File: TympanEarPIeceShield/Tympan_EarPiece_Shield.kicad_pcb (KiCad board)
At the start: 4 copper layers, 38 x 40 mm, 49 parts, among them J1 Tympan_SJ-3523-SMT-TR, J2 Tympan_SJ-3524-SMT-TR-PI, J3 USB_B_Mini, J4 USB_B_Mini, J5 Conn_01x01, J6 Conn_01x01, P1 CONN_01X06, P2 CONN_01X06, P3 CONN_01X06, P4 CONN_01X06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

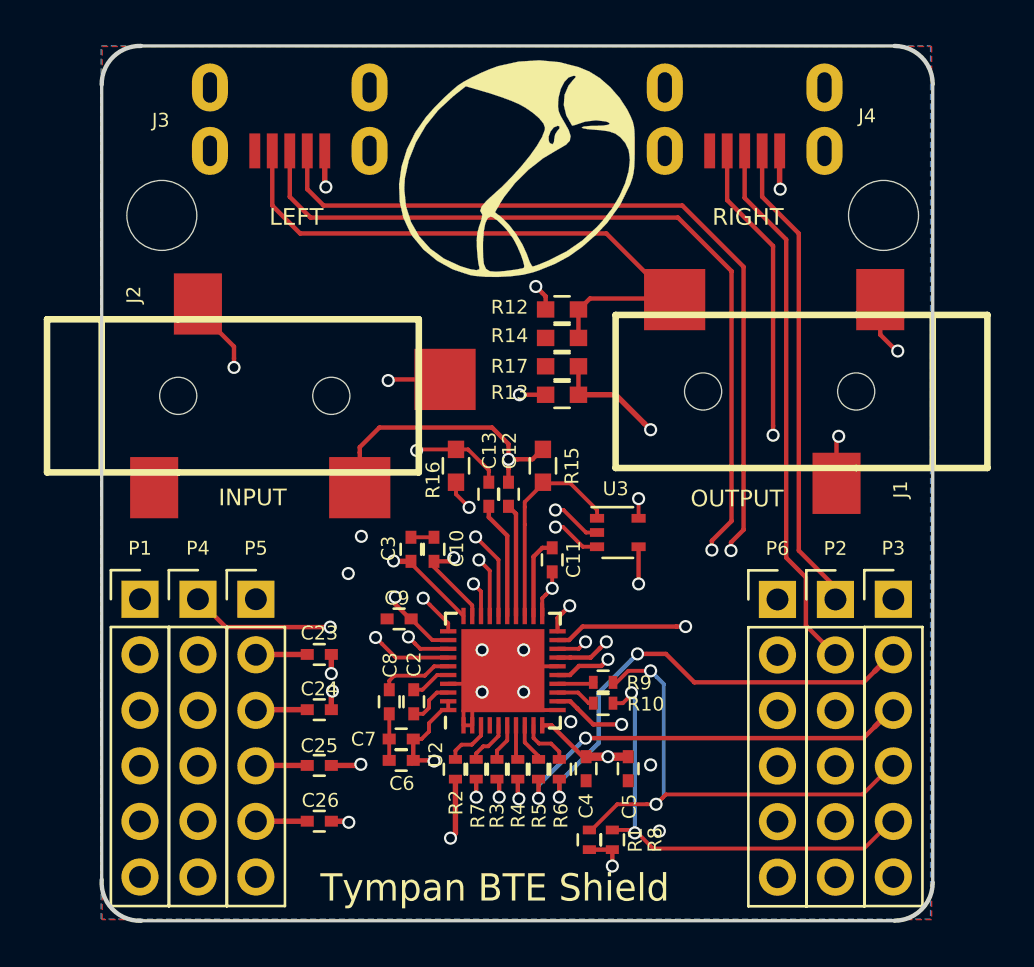
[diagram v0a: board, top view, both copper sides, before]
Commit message: Silk and audio jack positioning
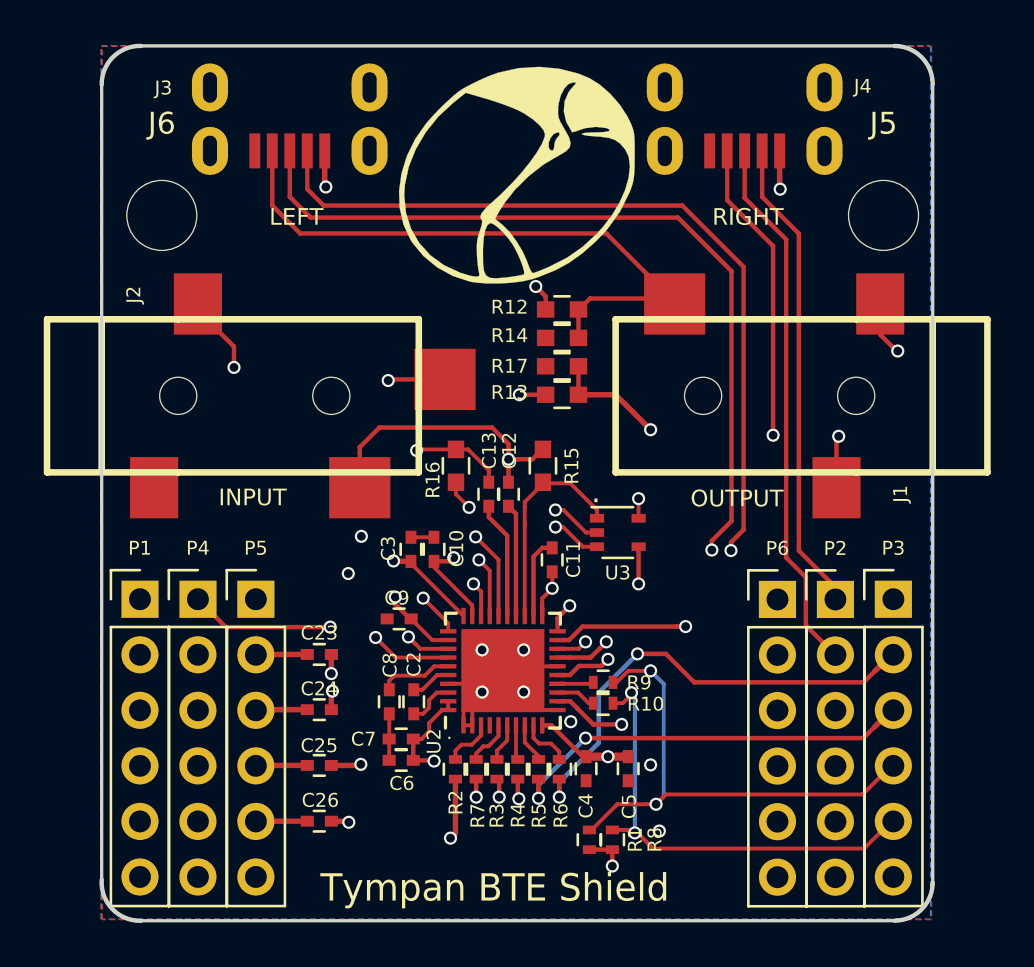
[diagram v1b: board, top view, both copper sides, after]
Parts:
- moved G*** 0.30 mm to (133.8, 52.4)
- moved J1 0.20 mm to (149.3, 62.5)
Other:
- board text added: "."
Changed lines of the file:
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@@
   (general
     (thickness 1.6)
-    (drawings 20)
+    (drawings 22)
     (tracks 496)
     (zones 0)
@@
   (layers
     (0 F.Cu signal)
-    (1 In1.Cu power)
-    (2 In2.Cu mixed)
-    (31 B.Cu signal)
+    (1 In1.Cu power hide)
+    (2 In2.Cu mixed hide)
+    (31 B.Cu signal hide)
     (32 B.Adhes user hide)
     (33 F.Adhes user hide)
     (34 B.Paste user)
     (35 F.Paste user)
-    (36 B.SilkS user)
+    (36 B.SilkS user hide)
     (37 F.SilkS user)
     (38 B.Mask user)
@@
   (module Tympan:USB_MINI_MOLEX_51387-0578 (layer F.Cu)
     (at 123.45 51.28)
-    (fp_text reference J3 (at -5.9 -1.4) (layer F.SilkS)
+    (fp_text reference J3 (at -5.775 -2.875) (layer F.SilkS)
       (effects (font (size 0.635 0.635) (thickness 0.127)))
     )
@@
   (module Tympan:USB_MINI_MOLEX_51387-0578 (layer F.Cu)
     (at 144.25 51.28)
-    (fp_text reference J4 (at 5.6 -1.6) (layer F.SilkS)
+    (fp_text reference J4 (at 5.4 -2.95) (layer F.SilkS)
       (effects (font (size 0.635 0.635) (thickness 0.127)))
     )
@@
   )
   (module Tympan:SJ-3523-SMT-TR (layer F.Cu)
-    (at 149.35 62.28 180)
+    (at 149.35 62.48 180)
     (attr smd)
     (fp_text reference J1 (at -2.032 -4.4831 90) (layer F.SilkS)
@@
   )
   (module Graphics:Tympan_LOGO (layer F.Cu)
-    (at 133.85 52.08)
+    (at 133.85 52.38)
     (attr smd)
     (fp_text reference G*** (at 0 0) (layer F.SilkS) hide
@@
     (tags "QFN 0.4")
     (attr smd)
-    (fp_text reference U2 (at -3.833 -3.0696 90) (layer F.SilkS)
+    (fp_text reference U2 (at -3.233 -3.1446 90) (layer F.SilkS)
       (effects (font (size 0.635 0.635) (thickness 0.127)))
     )
@@
     (tags "SOT-353 SC-70-5")
     (attr smd)
-    (fp_text reference U3 (at -0.1 -2) (layer F.SilkS)
+    (fp_text reference U3 (at 0 1.85) (layer F.SilkS)
       (effects (font (size 0.635 0.635) (thickness 0.127)))
     )
@@
     (tags "mounting hole 3.2mm no annular m3")
     (attr virtual)
-    (fp_text reference J5 (at 0.95 -2.85) (layer F.Fab)
+    (fp_text reference J5 (at 0 -4.2) (layer F.SilkS)
       (effects (font (size 1 1) (thickness 0.15)))
     )
@@
     (tags "mounting hole 3.2mm no annular m3")
     (attr virtual)
-    (fp_text reference J6 (at -1.65 -2.25) (layer F.Fab)
+    (fp_text reference J6 (at 0 -4.2) (layer F.SilkS)
       (effects (font (size 1 1) (thickness 0.15)))
     )
@@
     (pad 1 np_thru_hole circle (at 0 0) (size 3.2 3.2) (drill 3.2) (layers *.Cu *.Mask)
       (net 60 "Net-(J6-Pad1)"))
+  )
+  (gr_text . (at 130.75 77.88) (layer F.SilkS)
+    (effects (font (size 0.635 0.635) (thickness 0.127)))
+  )
+  (gr_text . (at 137.45 66.88) (layer F.SilkS)
+    (effects (font (size 1 1) (thickness 0.127)))
   )
   (gr_text LEFT (at 123.65 48.63) (layer B.SilkS)
@@
   (gr_line (start 151.1 46.48) (end 116.650536 46.479993) (angle 90) (layer Edge.Cuts) (width 0.15))
   (gr_line (start 152.85 84.73) (end 152.85 48.23) (angle 90) (layer Edge.Cuts) (width 0.15))
-  (gr_text "TYMPAN EARPIECE SHIELD" (at 133.85 69.28) (layer B.SilkS)
+  (gr_text "TYMPAN EARPIECE SHIELD" (at 133.85 69.58) (layer B.SilkS)
     (effects (font (size 1.524 1.524) (thickness 0.25)) (justify mirror))
   )
